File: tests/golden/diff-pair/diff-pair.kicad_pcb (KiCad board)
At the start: 2 copper layers, 38 x 40 mm, 7 parts, among them J1 USB_MICRO_B, J2 CONN_BRK_1X04

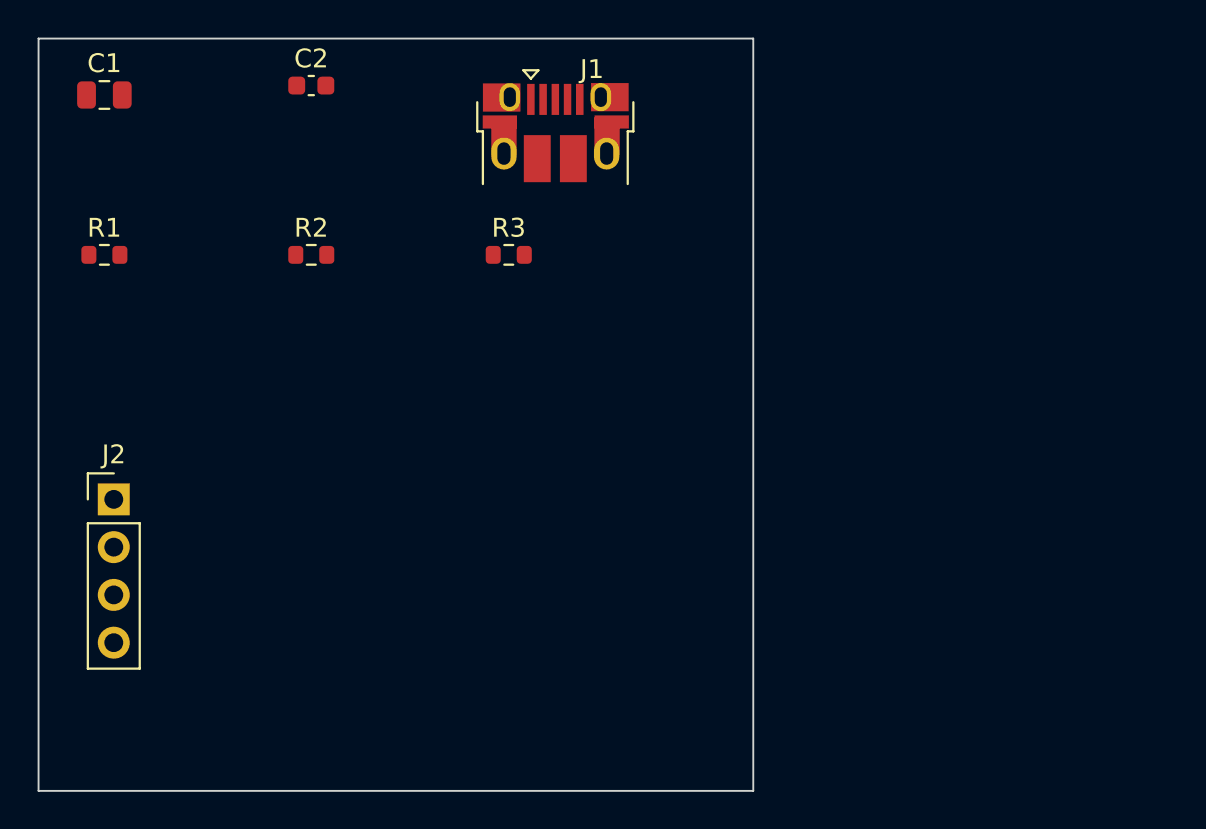
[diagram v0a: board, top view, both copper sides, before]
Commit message: M7d: differential pairs routed as pairs, with honest limits
A pair's impedance comes from the coupling between its halves, so routing them
independently routes something else with the same netlist. A pair is now tightened
once, as a single centre-line wide enough for both traces and the gap, then offset
to either side. The gap is correct everywhere by construction, corners included,
and the halves come out the same length: 43.00 mm each with 0.000 mm skew on the
new diff-pair example.

Where a class gives an impedance but no gap, the gap is estimated from the standard
edge-coupled microstrip formula and reported as an estimate. Where the target is
unreachable by spacing at all — a 0.34 mm trace on 0.7 mm of dielectric spans only
about 102-195 ohm however far apart the halves go — that is said plainly rather
than clamped, because the fix is the trace width or the stackup and clamping would
hide it.

Coupled routing checks its own output and falls back rather than shipping something
that only looks like a pair. It refuses an ambiguous pair, one that would need a
crossover, one that would be mostly fan-out, and one whose fan-out would not clear
an obstacle it then names. Both of usb-port's pairs refuse, each saying which.

That self-checking is the reason DRC stays clean: the tightener guarantees
clearance for the centre-line, but the fan-out at each end is constructed rather
than tightened, and an early version of it landed 27 violations including shorts.
Checking beats hoping.

All five examples now route with zero DRC violations and zero schematic-parity
issues. Also implements `region_mm` placement rules, which the model promised and
the placer had been ignoring.

Not built, and said so in the docs rather than left to be discovered: meander
insertion for length matching, and pair crossovers. Skew is measured and reported
against the budget; nothing yet closes it.

Co-Authored-By: Claude Opus 5 (1M context) <noreply@anthropic.com>
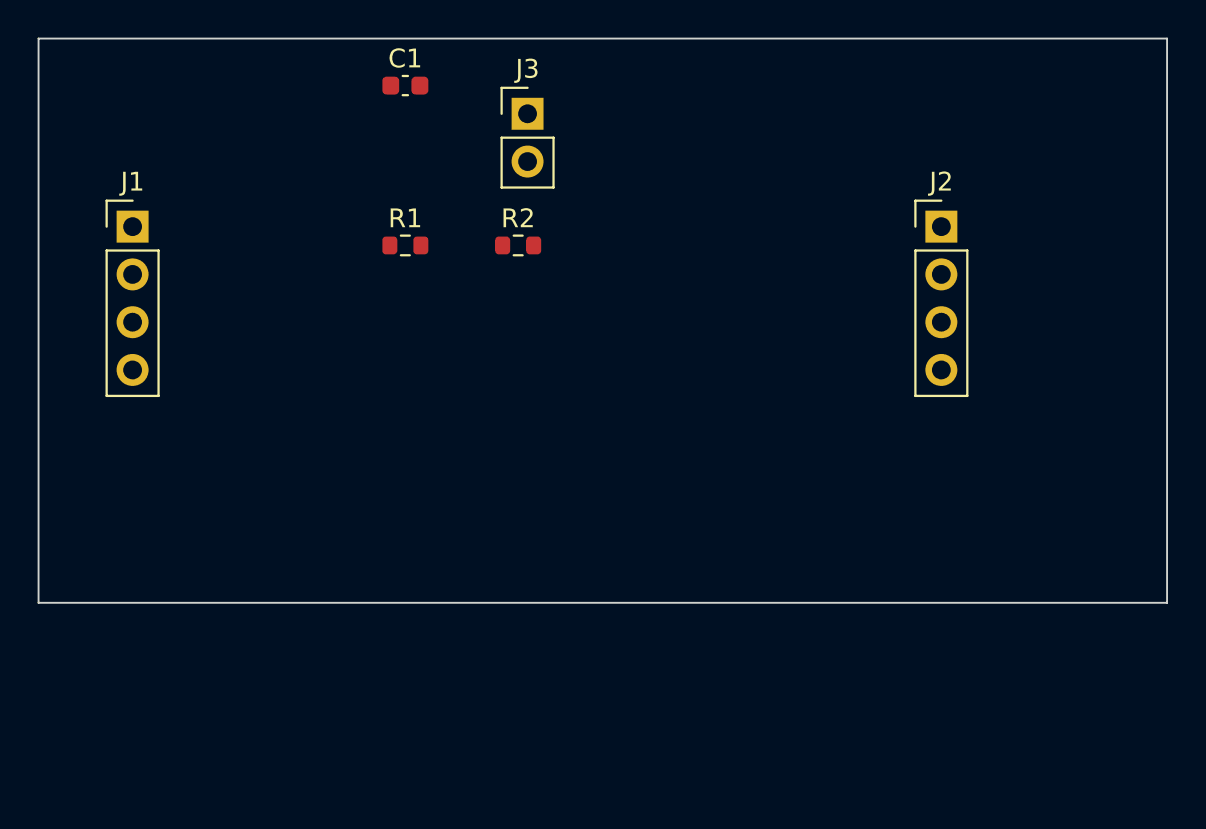
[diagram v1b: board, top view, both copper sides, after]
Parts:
- removed C2: C_100N_0603, Capacitor_SMD:C_0603_1608Metric
- removed R3: R_10K_0603, Resistor_SMD:R_0603_1608Metric
- added J3: CONN_PWR_1X02, Connector_PinHeader_2.54mm:PinHeader_1x02_P2.54mm_Vertical, F.Cu at (126.0, 104.0)
- C1: value C_10U_0805 -> C_100N_0603; footprint Capacitor_SMD:C_0805_2012Metric -> Capacitor_SMD:C_0603_1608Metric
- J1: value USB_MICRO_B -> CONN_BRK_1X04; footprint Connector_USB:USB_Micro-B_Amphenol_10103594-0001LF_Horizontal -> Connector_PinHeader_2.54mm:PinHeader_1x04_P2.54mm_Vertical
- R1, R2: value R_22R_0603 -> R_10K_0603
- moved J2 46.3 mm to (148.0, 110.0)
- moved J1 23.0 mm to (105.0, 110.0)
- moved C1 16.0 mm to (119.5, 102.5)
- moved R1 16.0 mm to (119.5, 111.0)
- moved R2 11.0 mm to (125.5, 111.0)
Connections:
- C1 pad 1: VBUS -> VCC
- J1 pad 1: VBUS -> GND
- J1 pad 2: USB_DM -> DIFF_P
- J1 pad 3: USB_DP -> DIFF_N
- J1 pad 4: ID -> VREF
- J2 pad 1: VBUS -> GND
- J2 pad 2: DEV_DP -> DIFF_P
- J2 pad 3: DEV_DM -> DIFF_N
- J2 pad 4: GND -> VCC
- R1 pad 1: USB_DP -> VCC
- R1 pad 2: DEV_DP -> VREF
- R2 pad 1: USB_DM -> VREF
- R2 pad 2: DEV_DM -> GND
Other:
- board size 38 x 40 mm -> 60 x 30 mm
